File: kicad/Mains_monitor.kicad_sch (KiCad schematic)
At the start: 34 parts, among them J1 Screw_Terminal_01x02, J2 Screw_Terminal_01x02, K1 SANYOU_SRD_Form_C, Q1 NPN, U1 HLW8032

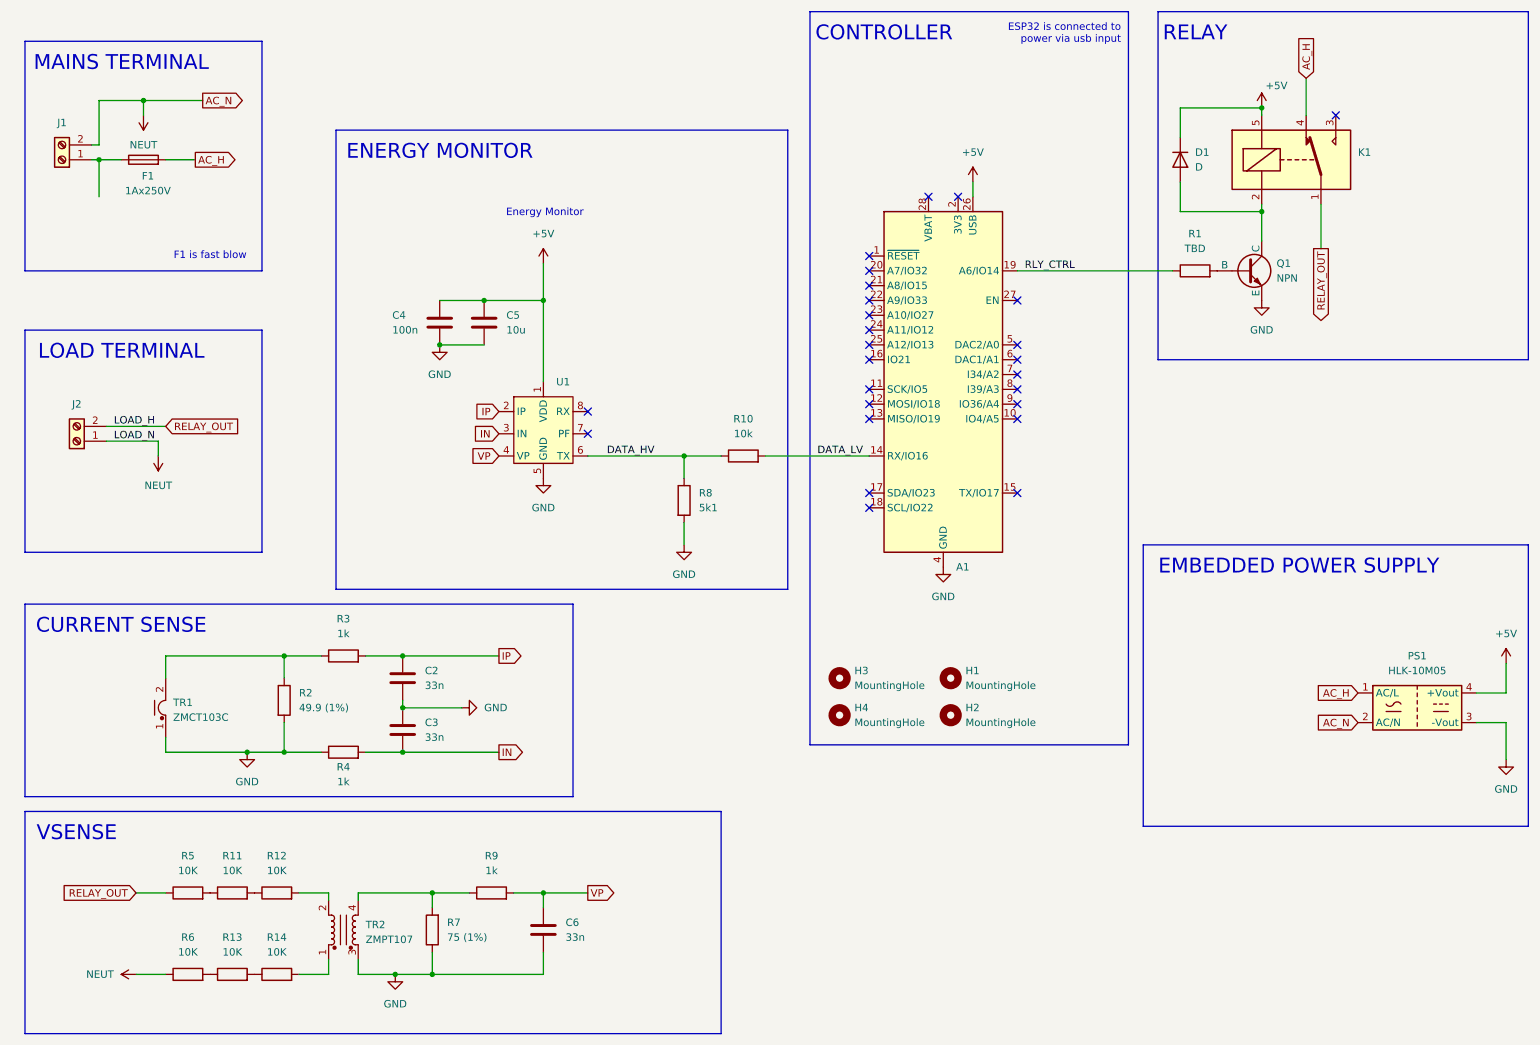
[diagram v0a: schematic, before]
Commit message: Clear ERC, and change Q1
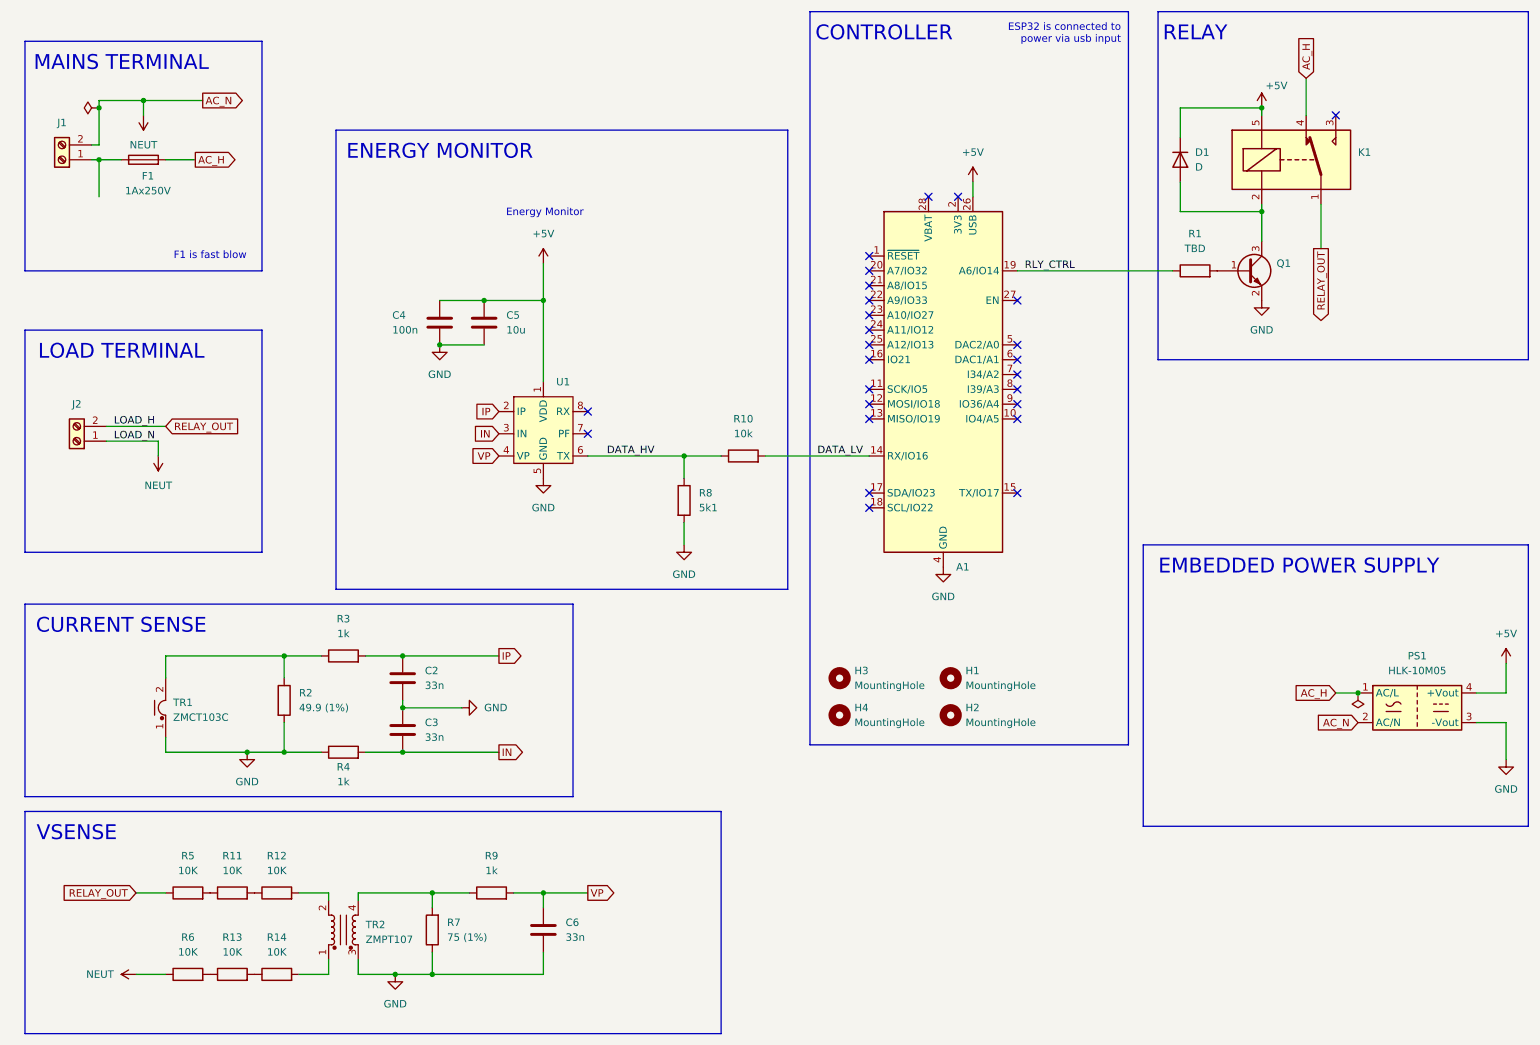
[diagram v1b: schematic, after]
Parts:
- removed Q1: NPN, Package_TO_SOT_THT:TO-92_Inline, symbol Simulation_SPICE:NPN
- added Q1: Q_NPN_BEC, Package_TO_SOT_THT:TO-92, symbol Device:Q_NPN_BEC
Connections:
- net GND: now also Q1.2 (E)
- net at R1.2: now also Q1.1 (B)
- net at D1.2 (A), K1.2: now also Q1.3 (C)
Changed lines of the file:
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@@
 	)
 	(junction
+		(at 250.19 138.43)
+		(diameter 0)
+		(color 0 0 0 0)
+	)
+	(junction
 		(at 134.62 97.79)
 		(diameter 0)
@@
 	)
 	(junction
+		(at 34.29 38.1)
+		(diameter 0)
+		(color 0 0 0 0)
+	)
+	(junction
 		(at 100.33 71.12)
 		(diameter 0)
@@
 	(wire
 		(pts
+			(xy 34.29 38.1) (xy 34.29 44.45)
+		)
+		(stroke
+			(width 0)
+			(type default)
+		)
+	)
+	(wire
+		(pts
 			(xy 270.51 143.51) (xy 275.59 143.51)
 		)
@@
 	(wire
 		(pts
-			(xy 34.29 36.83) (xy 34.29 44.45)
+			(xy 246.38 138.43) (xy 250.19 138.43)
+		)
+		(stroke
+			(width 0)
+			(type default)
+		)
+	)
+	(wire
+		(pts
+			(xy 34.29 36.83) (xy 34.29 38.1)
 		)
 		(stroke
@@
 	(global_label "AC_H"
 		(shape input)
-		(at 250.19 138.43 180)
+		(at 246.38 138.43 180)
 		(fields_autoplaced yes)
 		(effects
@@
 		)
 		(property "Intersheetrefs" "${INTERSHEET_REFS}"
-			(at 242.5481 138.43 0)
+			(at 238.7381 138.43 0)
 			(effects
 				(font
@@
 	)
 	(symbol
+		(lib_id "Device:Q_NPN_BEC")
+		(at 231.14 66.04 0)
+		(unit 1)
+		(exclude_from_sim no)
+		(in_bom yes)
+		(on_board yes)
+		(dnp no)
+		(fields_autoplaced yes)
+		(property "Reference" "Q1"
+			(at 236.22 64.7699 0)
+			(effects
+				(font
+					(size 1.27 1.27)
+				)
+				(justify left)
+			)
+		)
+		(property "Value" "Q_NPN_BEC"
+			(at 236.22 67.3099 0)
+			(effects
+				(font
+					(size 1.27 1.27)
+				)
+				(justify left)
+				(hide yes)
+			)
+		)
+		(property "Footprint" "Package_TO_SOT_THT:TO-92"
+			(at 236.22 63.5 0)
+			(effects
+				(font
+					(size 1.27 1.27)
+				)
+				(hide yes)
+			)
+		)
+		(property "Datasheet" "~"
+			(at 231.14 66.04 0)
+			(effects
+				(font
+					(size 1.27 1.27)
+				)
+				(hide yes)
+			)
+		)
+		(property "Description" "NPN transistor, base/emitter/collector"
+			(at 231.14 66.04 0)
+			(effects
+				(font
+					(size 1.27 1.27)
+				)
+				(hide yes)
+			)
+		)
+		(pin "1"
+		)
+		(pin "3"
+		)
+		(pin "2"
+		)
+		(instances
+			(project ""
+				(path "/825bfe7d-9d9b-4191-9855-e1cdfdd57fae"
+					(reference "Q1")
+					(unit 1)
+				)
+			)
+		)
+	)
+	(symbol
 		(lib_id "Device:R")
 		(at 57.15 186.69 90)
@@
 	)
 	(symbol
+		(lib_id "power:PWR_FLAG")
+		(at 250.19 138.43 180)
+		(unit 1)
+		(exclude_from_sim no)
+		(in_bom yes)
+		(on_board yes)
+		(dnp no)
+		(fields_autoplaced yes)
+		(property "Reference" "#FLG01"
+			(at 250.19 140.335 0)
+			(effects
+				(font
+					(size 1.27 1.27)
+				)
+				(hide yes)
+			)
+		)
+		(property "Value" "PWR_FLAG"
+			(at 250.19 143.51 0)
+			(effects
+				(font
+					(size 1.27 1.27)
+				)
+				(hide yes)
+			)
+		)
+		(property "Footprint" ""
+			(at 250.19 138.43 0)
+			(effects
+				(font
+					(size 1.27 1.27)
+				)
+				(hide yes)
+			)
+		)
+		(property "Datasheet" "~"
+			(at 250.19 138.43 0)
+			(effects
+				(font
+					(size 1.27 1.27)
+				)
+				(hide yes)
+			)
+		)
+		(property "Description" "Special symbol for telling ERC where power comes from"
+			(at 250.19 138.43 0)
+			(effects
+				(font
+					(size 1.27 1.27)
+				)
+				(hide yes)
+			)
+		)
+		(pin "1"
+		)
+		(instances
+			(project ""
+				(path "/825bfe7d-9d9b-4191-9855-e1cdfdd57fae"
+					(reference "#FLG01")
+					(unit 1)
+				)
+			)
+		)
+	)
+	(symbol
 		(lib_id "Device:R")
 		(at 64.77 186.69 90)
@@
 	)
 	(symbol
-		(lib_id "Simulation_SPICE:NPN")
-		(at 231.14 66.04 0)
+		(lib_id "power:+5V")
+		(at 184.15 50.8 0)
 		(unit 1)
 		(exclude_from_sim no)
@@
 		(dnp no)
 		(fields_autoplaced yes)
-		(property "Reference" "Q1"
-			(at 236.22 64.7699 0)
-			(effects
-				(font
-					(size 1.27 1.27)
-				)
-				(justify left)
-			)
-		)
-		(property "Value" "NPN"
-			(at 236.22 67.3099 0)
-			(effects
-				(font
-					(size 1.27 1.27)
-				)
-				(justify left)
-			)
-		)
-		(property "Footprint" "Package_TO_SOT_THT:TO-92_Inline"
-			(at 294.64 66.04 0)
-			(effects
-				(font
-					(size 1.27 1.27)
-				)
-				(hide yes)
-			)
-		)
-		(property "Datasheet" "https://ngspice.sourceforge.io/docs/ngspice-html-manual/manual.xhtml#cha_BJTs"
-			(at 294.64 66.04 0)
+		(property "Reference" "#PWR020"
+			(at 184.15 54.61 0)
 			(effects
 				(font
@@
 			)
 		)
-		(property "Description" "Bipolar transistor symbol for simulation only, substrate tied to the emitter"
-			(at 231.14 66.04 0)
+		(property "Value" "+5V"
+			(at 184.15 45.72 0)
 			(effects
 				(font
 					(size 1.27 1.27)
 				)
-				(hide yes)
 			)
 		)
-		(property "Sim.Device" "NPN"
-			(at 231.14 66.04 0)
+		(property "Footprint" ""
+			(at 184.15 50.8 0)
 			(effects
 				(font
@@
 			)
 		)
-		(property "Sim.Type" "GUMMELPOON"
-			(at 231.14 66.04 0)
+		(property "Datasheet" ""
+			(at 184.15 50.8 0)
 			(effects
 				(font
@@
 			)
 		)
-		(property "Sim.Pins" "1=C 2=B 3=E"
-			(at 231.14 66.04 0)
+		(property "Description" "Power symbol creates a global label with name \"+5V\""
+			(at 184.15 50.8 0)
 			(effects
 				(font
@@
 		(pin "1"
 		)
-		(pin "3"
-		)
-		(pin "2"
-		)
 		(instances
 			(project "Mains_monitor"
 				(path "/825bfe7d-9d9b-4191-9855-e1cdfdd57fae"
-					(reference "Q1")
+					(reference "#PWR020")
 					(unit 1)
 				)
@@
 	)
 	(symbol
-		(lib_id "power:+5V")
-		(at 184.15 50.8 0)
+		(lib_id "power:PWR_FLAG")
+		(at 34.29 38.1 90)
 		(unit 1)
 		(exclude_from_sim no)
@@
 		(dnp no)
 		(fields_autoplaced yes)
-		(property "Reference" "#PWR020"
-			(at 184.15 54.61 0)
+		(property "Reference" "#FLG02"
+			(at 32.385 38.1 0)
 			(effects
 				(font
@@
 			)
 		)
-		(property "Value" "+5V"
-			(at 184.15 45.72 0)
+		(property "Value" "PWR_FLAG"
+			(at 30.48 38.0999 90)
 			(effects
 				(font
 					(size 1.27 1.27)
 				)
+				(justify left)
+				(hide yes)
 			)
 		)
 		(property "Footprint" ""
-			(at 184.15 50.8 0)
+			(at 34.29 38.1 0)
 			(effects
 				(font
@@
 			)
 		)
-		(property "Datasheet" ""
-			(at 184.15 50.8 0)
+		(property "Datasheet" "~"
+			(at 34.29 38.1 0)
 			(effects
 				(font
@@
 			)
 		)
-		(property "Description" "Power symbol creates a global label with name \"+5V\""
-			(at 184.15 50.8 0)
+		(property "Description" "Special symbol for telling ERC where power comes from"
+			(at 34.29 38.1 0)
 			(effects
 				(font
@@
 		)
 		(instances
-			(project "Mains_monitor"
+			(project ""
 				(path "/825bfe7d-9d9b-4191-9855-e1cdfdd57fae"
-					(reference "#PWR020")
+					(reference "#FLG02")
 					(unit 1)
 				)

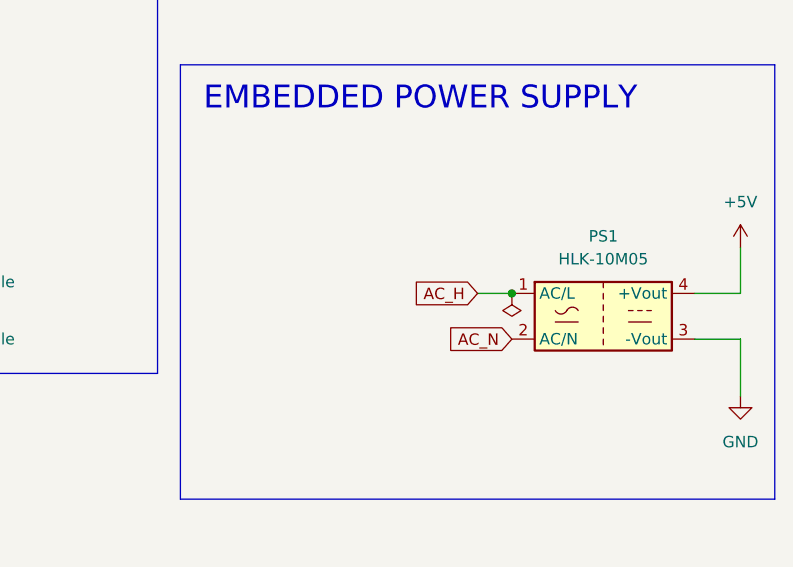
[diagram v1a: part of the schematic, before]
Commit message: added power supply fuse, increased high current trace size, Ready to order
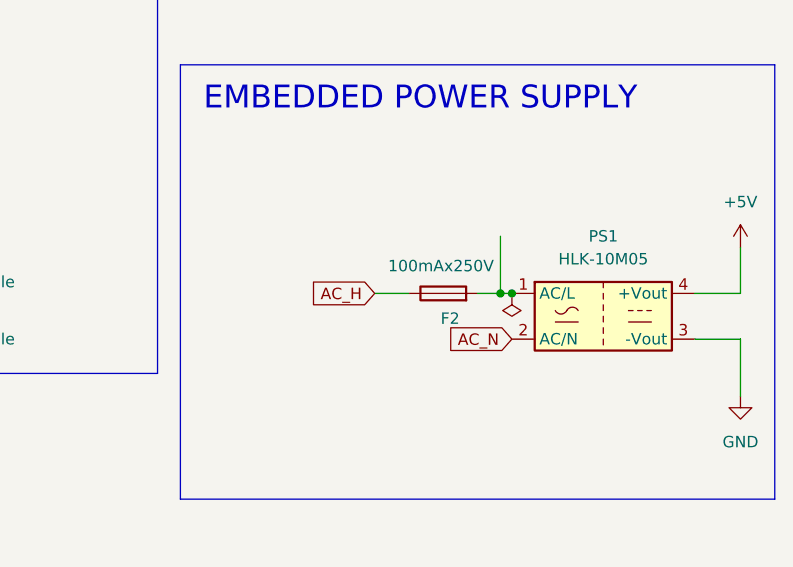
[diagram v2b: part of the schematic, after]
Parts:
- added F2: 100mAx250V, Fuse:Fuseholder_Clip-5x20mm_Bel_FC-203-22_Lateral_P17.80x5.00mm_D1.17mm_Horizontal, symbol Device:Fuse
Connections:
- net AC_H: now also F2.1; no longer PS1.1 (AC/L)
- new net: F2.2, PS1.1 (AC/L)
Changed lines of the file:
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@@
 	)
 	(junction
+		(at 248.92 138.43)
+		(diameter 0)
+		(color 0 0 0 0)
+	)
+	(junction
 		(at 134.62 97.79)
 		(diameter 0)
@@
 	(wire
 		(pts
+			(xy 248.92 138.43) (xy 250.19 138.43)
+		)
+		(stroke
+			(width 0)
+			(type default)
+		)
+	)
+	(wire
+		(pts
 			(xy 80.01 132.08) (xy 86.36 132.08)
 		)
@@
 	(wire
 		(pts
-			(xy 270.51 143.51) (xy 275.59 143.51)
+			(xy 248.92 132.08) (xy 248.92 138.43)
 		)
 		(stroke
@@
 	(wire
 		(pts
-			(xy 45.72 146.05) (xy 45.72 148.59)
+			(xy 270.51 143.51) (xy 275.59 143.51)
 		)
 		(stroke
@@
 	(wire
 		(pts
-			(xy 86.36 139.7) (xy 86.36 140.97)
+			(xy 45.72 146.05) (xy 45.72 148.59)
 		)
 		(stroke
@@
 	(wire
 		(pts
-			(xy 246.38 138.43) (xy 250.19 138.43)
+			(xy 86.36 139.7) (xy 86.36 140.97)
 		)
 		(stroke
@@
 	(wire
 		(pts
+			(xy 246.38 138.43) (xy 248.92 138.43)
+		)
+		(stroke
+			(width 0)
+			(type default)
+		)
+	)
+	(wire
+		(pts
 			(xy 134.62 97.79) (xy 134.62 101.6)
 		)
@@
 	(wire
 		(pts
+			(xy 234.95 138.43) (xy 238.76 138.43)
+		)
+		(stroke
+			(width 0)
+			(type default)
+		)
+	)
+	(wire
+		(pts
 			(xy 241.3 33.02) (xy 241.3 39.37)
 		)
@@
 	(global_label "AC_H"
 		(shape input)
-		(at 246.38 138.43 180)
+		(at 234.95 138.43 180)
 		(fields_autoplaced yes)
 		(effects
@@
 		)
 		(property "Intersheetrefs" "${INTERSHEET_REFS}"
-			(at 238.7381 138.43 0)
+			(at 227.3081 138.43 0)
 			(effects
 				(font
@@
 		(length 2.54)
 		(shape round)
+		(at 248.92 132.08 0)
+		(fields_autoplaced yes)
+		(effects
+			(font
+				(size 1.27 1.27)
+			)
+			(justify left bottom)
+		)
+		(property "Netclass" "120V"
+			(at 249.6185 129.54 0)
+			(effects
+				(font
+					(size 1.27 1.27)
+					(italic yes)
+				)
+				(justify left)
+			)
+		)
+	)
+	(netclass_flag ""
+		(length 2.54)
+		(shape round)
 		(at 44.45 92.71 0)
 		(fields_autoplaced yes)
@@
 					(unit 1)
 				)
+			)
+		)
+	)
+	(symbol
+		(lib_id "Device:Fuse")
+		(at 242.57 138.43 90)
+		(unit 1)
+		(exclude_from_sim no)
+		(in_bom yes)
+		(on_board yes)
+		(dnp no)
+		(property "Reference" "F2"
+			(at 243.332 141.224 90)
+			(effects
+				(font
+					(size 1.27 1.27)
+				)
+			)
+		)
+		(property "Value" "100mAx250V"
+			(at 242.316 135.382 90)
+			(effects
+				(font
+					(size 1.27 1.27)
+				)
+			)
+		)
+		(property "Footprint" "Fuse:Fuseholder_Clip-5x20mm_Bel_FC-203-22_Lateral_P17.80x5.00mm_D1.17mm_Horizontal"
+			(at 242.57 140.208 90)
+			(effects
+				(font
+					(size 1.27 1.27)
+				)
+				(hide yes)
+			)
+		)
+		(property "Datasheet" "~"
+			(at 242.57 138.43 0)
+			(effects
+				(font
+					(size 1.27 1.27)
+				)
+				(hide yes)
+			)
+		)
+		(property "Description" "Fuse"
+			(at 242.57 138.43 0)
+			(effects
+				(font
+					(size 1.27 1.27)
+				)
+				(hide yes)
+			)
+		)
+		(pin "1"
+		)
+		(pin "2"
+		)
+		(instances
+			(project "Mains_monitor"
+				(path "/825bfe7d-9d9b-4191-9855-e1cdfdd57fae"
+					(reference "F2")
+					(unit 1)
+				)
